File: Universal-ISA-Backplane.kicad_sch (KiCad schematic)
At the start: 0 parts

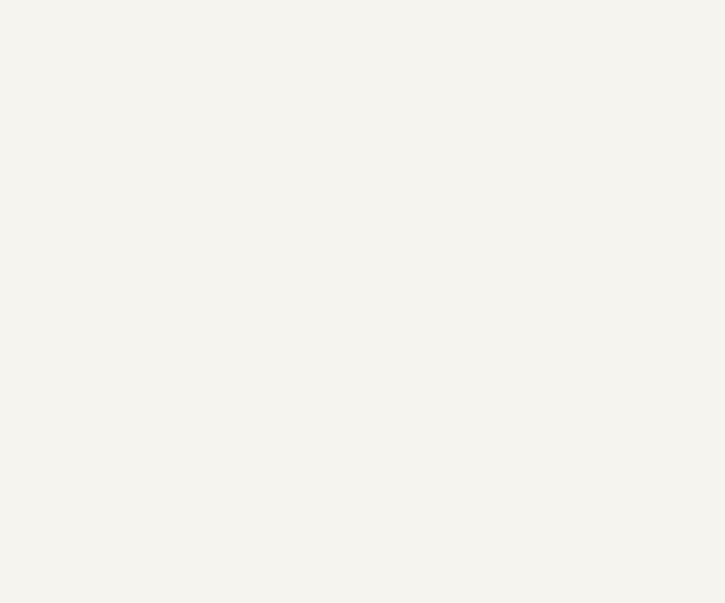
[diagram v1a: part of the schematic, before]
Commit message: PC/104 and ISA connector fixes
And further development
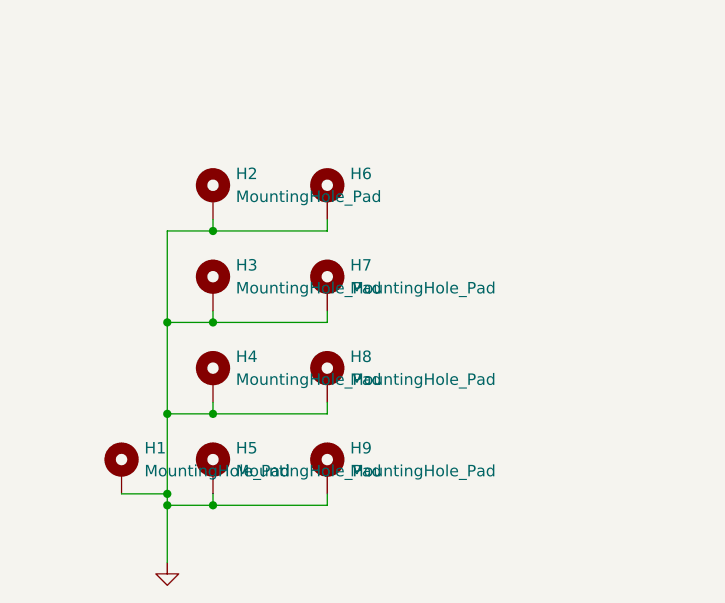
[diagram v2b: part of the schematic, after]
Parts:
- added H1, H2, H3, H4, H5, H7, H8, H9: MountingHole_Pad, symbol Mechanical:MountingHole_Pad
- added H6: (no value), symbol Mechanical:MountingHole_Pad
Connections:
- new net GND: H1.1, H2.1, H3.1, H4.1, H5.1, H6.1, H7.1, H8.1, H9.1

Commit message: Kicad resave fixup
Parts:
- H1, H2, H3, H4, H5, H7, H8, H9: value MountingHole_Pad -> (none)
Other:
- moved on the sheet: H1, H2, H3, H4, H5, H6, H7, H8, H9

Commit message: Just another resave
Not sure why eeschema changed the values and footprints of H1 - H9
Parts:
- H1, H2, H3, H4, H5, H6, H7, H8, H9: value (none) -> MountingHole_Pad; footprint (none) -> MountingHole:MountingHole_4mm_Pad_TopBottom
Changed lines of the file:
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@@
       (effects (font (size 1.27 1.27)) (justify left))
     )
-    (property "Value" "" (id 1) (at 49.53 154.9399 0)
+    (property "Value" "MountingHole_Pad" (id 1) (at 49.53 154.9399 0)
       (effects (font (size 1.27 1.27)) (justify left) hide)
     )
-    (property "Footprint" "" (id 2) (at 46.99 154.94 0)
+    (property "Footprint" "MountingHole:MountingHole_4mm_Pad_TopBottom" (id 2) (at 46.99 154.94 0)
       (effects (font (size 1.27 1.27)) hide)
     )
@@
       (effects (font (size 1.27 1.27)) (justify left))
     )
-    (property "Value" "" (id 1) (at 64.77 165.0999 0)
+    (property "Value" "MountingHole_Pad" (id 1) (at 64.77 165.0999 0)
       (effects (font (size 1.27 1.27)) (justify left) hide)
     )
-    (property "Footprint" "" (id 2) (at 62.23 165.1 0)
+    (property "Footprint" "MountingHole:MountingHole_4mm_Pad_TopBottom" (id 2) (at 62.23 165.1 0)
       (effects (font (size 1.27 1.27)) hide)
     )
@@
       (effects (font (size 1.27 1.27)) (justify left))
     )
-    (property "Value" "" (id 1) (at 29.21 154.9399 0)
+    (property "Value" "MountingHole_Pad" (id 1) (at 29.21 154.9399 0)
       (effects (font (size 1.27 1.27)) (justify left) hide)
     )
-    (property "Footprint" "" (id 2) (at 26.67 154.94 0)
+    (property "Footprint" "MountingHole:MountingHole_4mm_Pad_TopBottom" (id 2) (at 26.67 154.94 0)
       (effects (font (size 1.27 1.27)) hide)
     )
@@
       (effects (font (size 1.27 1.27)) (justify left))
     )
-    (property "Value" "" (id 1) (at 44.45 165.0999 0)
+    (property "Value" "MountingHole_Pad" (id 1) (at 44.45 165.0999 0)
       (effects (font (size 1.27 1.27)) (justify left) hide)
     )
-    (property "Footprint" "" (id 2) (at 41.91 165.1 0)
+    (property "Footprint" "MountingHole:MountingHole_4mm_Pad_TopBottom" (id 2) (at 41.91 165.1 0)
       (effects (font (size 1.27 1.27)) hide)
     )
@@
       (effects (font (size 1.27 1.27)) (justify left))
     )
-    (property "Value" "" (id 1) (at 69.85 154.9399 0)
+    (property "Value" "MountingHole_Pad" (id 1) (at 69.85 154.9399 0)
       (effects (font (size 1.27 1.27)) (justify left) hide)
     )
-    (property "Footprint" "" (id 2) (at 67.31 154.94 0)
+    (property "Footprint" "MountingHole:MountingHole_4mm_Pad_TopBottom" (id 2) (at 67.31 154.94 0)
       (effects (font (size 1.27 1.27)) hide)
     )
@@
       (effects (font (size 1.27 1.27)) (justify left))
     )
-    (property "Value" "" (id 1) (at 59.69 154.9399 0)
+    (property "Value" "MountingHole_Pad" (id 1) (at 59.69 154.9399 0)
       (effects (font (size 1.27 1.27)) (justify left) hide)
     )
-    (property "Footprint" "" (id 2) (at 57.15 154.94 0)
+    (property "Footprint" "MountingHole:MountingHole_4mm_Pad_TopBottom" (id 2) (at 57.15 154.94 0)
       (effects (font (size 1.27 1.27)) hide)
     )
@@
       (effects (font (size 1.27 1.27)) (justify right))
     )
-    (property "Value" "" (id 1) (at 39.37 154.9399 0)
+    (property "Value" "MountingHole_Pad" (id 1) (at 39.37 154.9399 0)
       (effects (font (size 1.27 1.27)) (justify right) hide)
     )
-    (property "Footprint" "" (id 2) (at 36.83 154.94 0)
+    (property "Footprint" "MountingHole:MountingHole_4mm_Pad_TopBottom" (id 2) (at 36.83 154.94 0)
       (effects (font (size 1.27 1.27)) hide)
     )
@@
       (effects (font (size 1.27 1.27)) (justify left))
     )
-    (property "Value" "" (id 1) (at 34.29 165.0999 0)
+    (property "Value" "MountingHole_Pad" (id 1) (at 34.29 165.0999 0)
       (effects (font (size 1.27 1.27)) (justify left) hide)
     )
-    (property "Footprint" "" (id 2) (at 31.75 165.1 0)
+    (property "Footprint" "MountingHole:MountingHole_4mm_Pad_TopBottom" (id 2) (at 31.75 165.1 0)
       (effects (font (size 1.27 1.27)) hide)
     )
@@
       (effects (font (size 1.27 1.27)) (justify left))
     )
-    (property "Value" "" (id 1) (at 54.61 165.0999 0)
+    (property "Value" "MountingHole_Pad" (id 1) (at 54.61 165.0999 0)
       (effects (font (size 1.27 1.27)) (justify left) hide)
     )
-    (property "Footprint" "" (id 2) (at 52.07 165.1 0)
+    (property "Footprint" "MountingHole:MountingHole_4mm_Pad_TopBottom" (id 2) (at 52.07 165.1 0)
       (effects (font (size 1.27 1.27)) hide)
     )
